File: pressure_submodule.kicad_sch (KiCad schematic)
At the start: 17 parts, among them J12 Conn_01x04, Q10 BSZ0902NSATMA1, U11 INA180

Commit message: Routing basics done
All layers + the basic layout is already set
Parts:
- renumbered D11 to D2, F19 to F1, F20 to F2, J12 to J3, JP55 to JP1, JP56 to JP2, JP59 to JP5, JP60 to JP6, Q10 to Q1, R64 to R1, R65 to R2, R66 to R3, R67 to R4, R68 to R5, R69 to R6, R70 to R7, U11 to U2
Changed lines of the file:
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@@
   (symbol (lib_id "Connector_Generic:Conn_01x04") (at 241.3 89.281 0)
     (in_bom yes) (on_board yes)
-    (property "Reference" "J12" (id 0) (at 243.332 89.4842 0)
+    (property "Reference" "J3" (id 0) (at 243.332 89.4842 0)
       (effects (font (size 1.27 1.27)) (justify left))
     )
@@
   (symbol (lib_id "Jumper:Jumper_2_Open") (at 241.3 124.206 270)
     (in_bom yes) (on_board yes)
-    (property "Reference" "JP59" (id 0) (at 238.125 124.206 90)
+    (property "Reference" "JP5" (id 0) (at 238.125 124.206 90)
       (effects (font (size 1.27 1.27)) (justify left))
     )
@@
   (symbol (lib_id "Jumper:Jumper_2_Open") (at 241.3 138.176 270)
     (in_bom yes) (on_board yes)
-    (property "Reference" "JP60" (id 0) (at 237.49 138.176 90)
+    (property "Reference" "JP6" (id 0) (at 237.49 138.176 90)
       (effects (font (size 1.27 1.27)) (justify left))
     )
@@
   (symbol (lib_id "power:+3.3V") (at 213.868 75.946 0)
     (in_bom yes) (on_board yes)
-    (property "Reference" "#PWR089" (id 0) (at 213.868 79.756 0)
+    (property "Reference" "#PWR0105" (id 0) (at 213.868 79.756 0)
       (effects (font (size 1.27 1.27)) hide)
     )
@@
   (symbol (lib_id "Device:Polyfuse") (at 223.393 81.153 0)
     (in_bom yes) (on_board yes) (fields_autoplaced)
-    (property "Reference" "F20" (id 0) (at 225.806 79.8829 0)
+    (property "Reference" "F2" (id 0) (at 225.806 79.8829 0)
       (effects (font (size 1.27 1.27)) (justify left))
     )
@@
   (symbol (lib_id "Device:R") (at 212.09 138.811 0)
     (in_bom yes) (on_board yes)
-    (property "Reference" "R70" (id 0) (at 205.74 137.541 0)
+    (property "Reference" "R7" (id 0) (at 205.74 137.541 0)
       (effects (font (size 1.27 1.27)) (justify left))
     )
@@
   (symbol (lib_id "power:+3.3V") (at 241.3 117.856 0)
     (in_bom yes) (on_board yes)
-    (property "Reference" "#PWR092" (id 0) (at 241.3 121.666 0)
+    (property "Reference" "#PWR0108" (id 0) (at 241.3 121.666 0)
       (effects (font (size 1.27 1.27)) hide)
     )
@@
   (symbol (lib_id "Device:Polyfuse") (at 213.868 81.28 0)
     (in_bom yes) (on_board yes) (fields_autoplaced)
-    (property "Reference" "F19" (id 0) (at 216.281 80.0099 0)
+    (property "Reference" "F1" (id 0) (at 216.281 80.0099 0)
       (effects (font (size 1.27 1.27)) (justify left))
     )
@@
   (symbol (lib_id "power:GNDA") (at 223.52 145.796 0)
     (in_bom yes) (on_board yes)
-    (property "Reference" "#PWR091" (id 0) (at 223.52 152.146 0)
+    (property "Reference" "#PWR0107" (id 0) (at 223.52 152.146 0)
       (effects (font (size 1.27 1.27)) hide)
     )
@@
   (symbol (lib_id "Jumper:Jumper_2_Open") (at 189.865 72.771 0)
     (in_bom yes) (on_board yes)
-    (property "Reference" "JP55" (id 0) (at 188.595 69.596 0)
+    (property "Reference" "JP1" (id 0) (at 188.595 69.596 0)
       (effects (font (size 1.27 1.27)) (justify left))
     )
@@
   (symbol (lib_id "power:+24V") (at 223.393 75.946 0)
     (in_bom yes) (on_board yes)
-    (property "Reference" "#PWR090" (id 0) (at 223.393 79.756 0)
+    (property "Reference" "#PWR0106" (id 0) (at 223.393 79.756 0)
       (effects (font (size 1.27 1.27)) hide)
     )
@@
   (symbol (lib_id "Jumper:Jumper_2_Open") (at 212.09 108.331 270)
     (in_bom yes) (on_board yes)
-    (property "Reference" "JP56" (id 0) (at 210.185 108.331 90)
+    (property "Reference" "JP2" (id 0) (at 210.185 108.331 90)
       (effects (font (size 1.27 1.27)) (justify left))
     )
@@
   (symbol (lib_id "Device:R") (at 178.435 97.536 0)
     (in_bom yes) (on_board yes)
-    (property "Reference" "R64" (id 0) (at 173.355 95.631 0)
+    (property "Reference" "R1" (id 0) (at 173.355 95.631 0)
       (effects (font (size 1.27 1.27)) (justify left))
     )
@@
   (symbol (lib_id "Device:R") (at 201.295 99.441 0)
     (in_bom yes) (on_board yes)
-    (property "Reference" "R66" (id 0) (at 196.215 97.536 0)
+    (property "Reference" "R3" (id 0) (at 196.215 97.536 0)
       (effects (font (size 1.27 1.27)) (justify left))
     )
@@
   (symbol (lib_id "Device:R") (at 178.435 107.696 0)
     (in_bom yes) (on_board yes)
-    (property "Reference" "R65" (id 0) (at 173.355 105.791 0)
+    (property "Reference" "R2" (id 0) (at 173.355 105.791 0)
       (effects (font (size 1.27 1.27)) (justify left))
     )
@@
   (symbol (lib_id "Device:R") (at 212.09 128.016 0)
     (in_bom yes) (on_board yes)
-    (property "Reference" "R69" (id 0) (at 205.74 126.746 0)
+    (property "Reference" "R6" (id 0) (at 205.74 126.746 0)
       (effects (font (size 1.27 1.27)) (justify left))
     )
@@
   (symbol (lib_id "Device:D") (at 231.14 133.096 270)
     (in_bom yes) (on_board yes)
-    (property "Reference" "D11" (id 0) (at 233.1466 131.9276 90)
+    (property "Reference" "D2" (id 0) (at 233.1466 131.9276 90)
       (effects (font (size 1.27 1.27)) (justify left))
     )
@@
   (symbol (lib_id "power:GNDA") (at 178.435 112.776 0)
     (in_bom yes) (on_board yes)
-    (property "Reference" "#PWR085" (id 0) (at 178.435 119.126 0)
+    (property "Reference" "#PWR0101" (id 0) (at 178.435 119.126 0)
       (effects (font (size 1.27 1.27)) hide)
     )
@@
   (symbol (lib_id "IOB-rescue:INA180-TXV_Library_Symbols") (at 187.325 91.821 0) (mirror y)
     (in_bom yes) (on_board yes)
-    (property "Reference" "U11" (id 0) (at 184.15 87.376 0))
+    (property "Reference" "U2" (id 0) (at 184.15 87.376 0))
     (property "Value" "INA180" (id 1) (at 184.15 95.631 0))
     (property "Footprint" "Package_TO_SOT_SMD:SOT-23-6" (id 2) (at 186.055 90.551 0)
@@
   (symbol (lib_id "IOB-rescue:BSZ0902NSATMA1-TXV_Library_Symbols") (at 222.25 133.731 0)
     (in_bom yes) (on_board yes)
-    (property "Reference" "Q10" (id 0) (at 226.187 133.731 0)
+    (property "Reference" "Q1" (id 0) (at 226.187 133.731 0)
       (effects (font (size 1.27 1.27)) (justify left))
     )
@@
   (symbol (lib_id "Device:R") (at 212.09 93.726 0)
     (in_bom yes) (on_board yes)
-    (property "Reference" "R68" (id 0) (at 207.01 92.456 0)
+    (property "Reference" "R5" (id 0) (at 207.01 92.456 0)
       (effects (font (size 1.27 1.27)) (justify left))
     )
@@
   (symbol (lib_id "power:+3.3V") (at 212.09 122.301 0)
     (in_bom yes) (on_board yes)
-    (property "Reference" "#PWR088" (id 0) (at 212.09 126.111 0)
+    (property "Reference" "#PWR0104" (id 0) (at 212.09 126.111 0)
       (effects (font (size 1.27 1.27)) hide)
     )
@@
   (symbol (lib_id "power:GNDA") (at 189.865 105.791 0)
     (in_bom yes) (on_board yes)
-    (property "Reference" "#PWR087" (id 0) (at 189.865 112.141 0)
+    (property "Reference" "#PWR0103" (id 0) (at 189.865 112.141 0)
       (effects (font (size 1.27 1.27)) hide)
     )
@@
   (symbol (lib_id "Device:R") (at 203.835 133.731 90)
     (in_bom yes) (on_board yes)
-    (property "Reference" "R67" (id 0) (at 203.2 131.826 90)
+    (property "Reference" "R4" (id 0) (at 203.2 131.826 90)
       (effects (font (size 1.27 1.27)) (justify left))
     )
@@
   (symbol (lib_id "power:+3.3V") (at 189.865 82.931 0)
     (in_bom yes) (on_board yes)
-    (property "Reference" "#PWR086" (id 0) (at 189.865 86.741 0)
-      (effects (font (size 1.27 1.27)) hide)
-    )
+    (property "Reference" "#PWR0102" (id 0) (at 189.865 86.741 0)
+      (effects (font (size 1.27 1.27)) hide)
+    )

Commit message: Ready for first review
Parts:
- renumbered D2 to D13, F1 to F23, F2 to F24, J3 to J14, JP1 to JP67, JP2 to JP68, JP5 to JP71, JP6 to JP72, Q1 to Q12, R1 to R78, R2 to R79, R3 to R80, R4 to R81, R5 to R82, R6 to R83, R7 to R84, U2 to U13

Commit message: 5V SMPS Layout Edit
The 5V SMPS Layout was changed to a similar one as in the IOB V2
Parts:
- renumbered D13 to D2, F23 to F1, F24 to F2, J14 to J3, JP67 to JP1, JP68 to JP2, JP71 to JP5, JP72 to JP6, Q12 to Q1, R78 to R1, R79 to R2, R80 to R3, R81 to R4, R82 to R5, R83 to R6, R84 to R7, U13 to U2

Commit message: Connection layout set
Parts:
- renumbered D2 to D8, F1 to F13, F2 to F14, J3 to J9, JP1 to JP37, JP2 to JP38, JP5 to JP41, JP6 to JP42, Q1 to Q7, R1 to R43, R2 to R44, R3 to R45, R4 to R46, R5 to R47, R6 to R48, R7 to R49, U2 to U8

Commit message: Layout WIP
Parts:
- renumbered D8 to D2, F13 to F1, F14 to F2, J9 to J3, JP37 to JP1, JP38 to JP2, JP41 to JP5, JP42 to JP6, Q7 to Q1, R43 to R1, R44 to R2, R45 to R3, R46 to R4, R47 to R5, R48 to R6, R49 to R7, U8 to U2

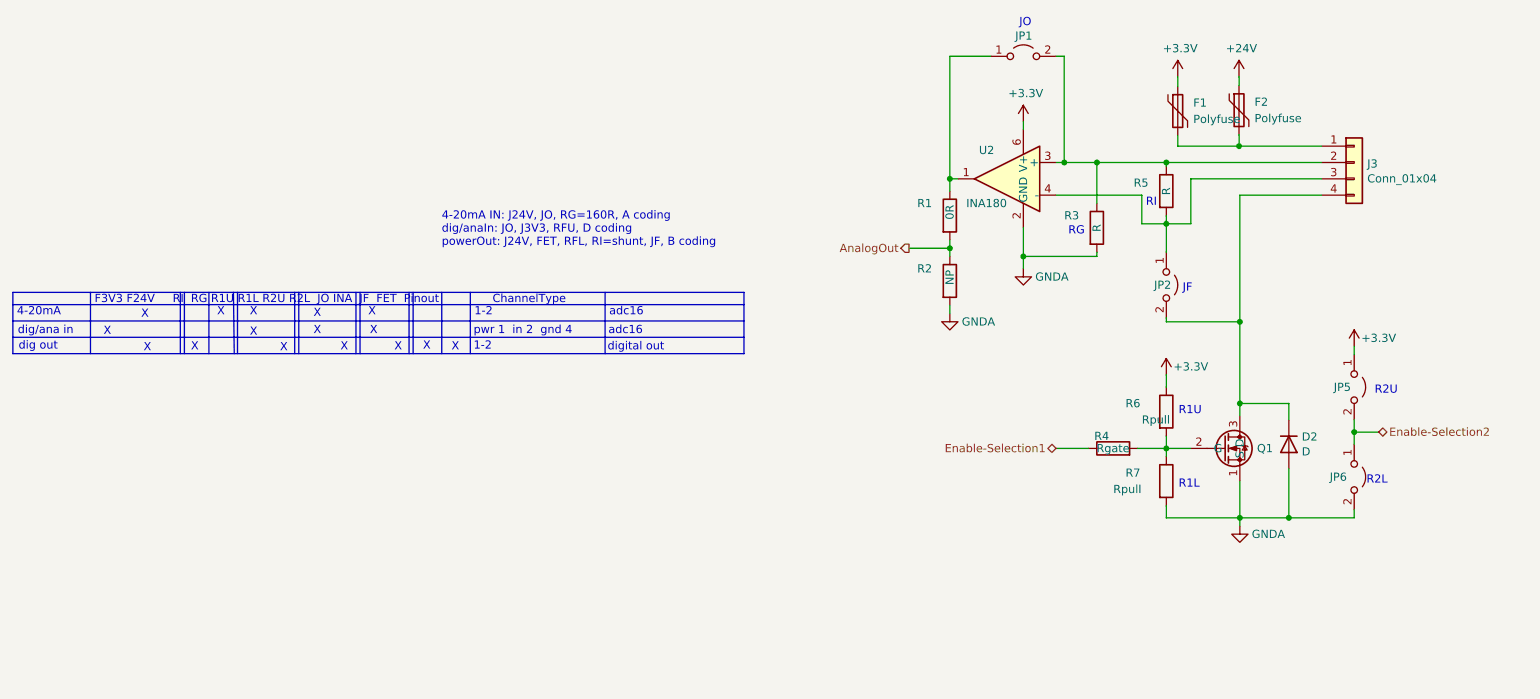
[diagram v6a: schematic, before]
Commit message: Layer change + INA change + SPI 24V added + minor changes
Stitching is still missing
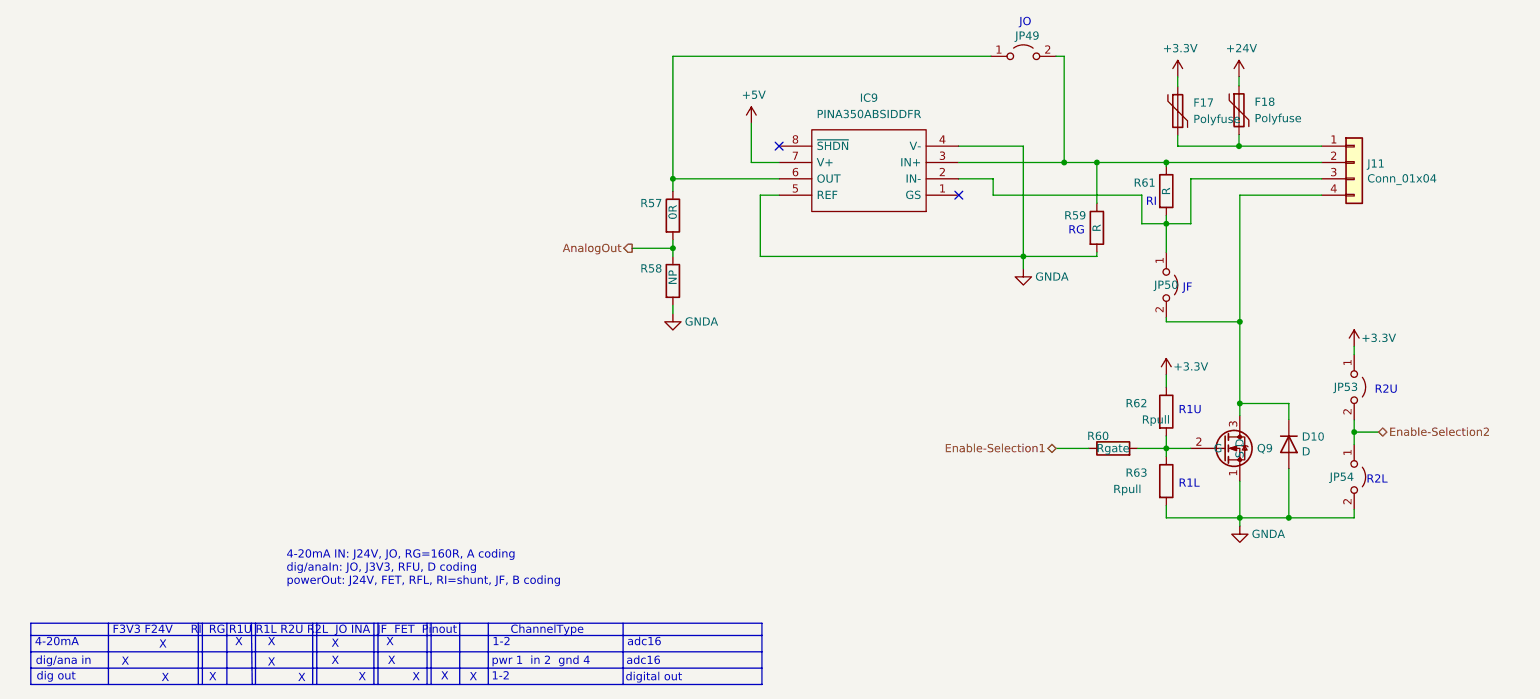
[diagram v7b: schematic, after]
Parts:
- removed U2: INA180, Package_TO_SOT_SMD:SOT-23-6, symbol IOB-rescue:INA180-TXV_Library_Symbols
- added IC9: PINA350ABSIDDFR, SOT65P280X110-8N, symbol PINA350ABSIDDFR:PINA350ABSIDDFR
- renumbered D2 to D10, F1 to F17, F2 to F18, J3 to J11, JP1 to JP49, JP2 to JP50, JP5 to JP53, JP6 to JP54, Q1 to Q9, R1 to R57, R2 to R58, R3 to R59, R4 to R60, R5 to R61, R6 to R62, R7 to R63
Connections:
- net GNDA: now also IC9.4 (V-), IC9.5 (REF)
- net at J11.2 (Pin_2), JP49.2 (B), R59.1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: now also IC9.3 (IN+)
- net at J11.3 (Pin_3), JP50.1 (A), R61.2: now also IC9.2 (IN-)
- net at JP49.1 (A), R57.1: now also IC9.6 (OUT)
- new net +5V: IC9.7 (V+)
- no-connect marks 0 -> 2
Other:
- moved on the sheet: R57, R58
